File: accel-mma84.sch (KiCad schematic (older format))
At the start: 9 parts, among them J2 CONN_01X10, J3 CONN_01X02, U1 MMA8452Q

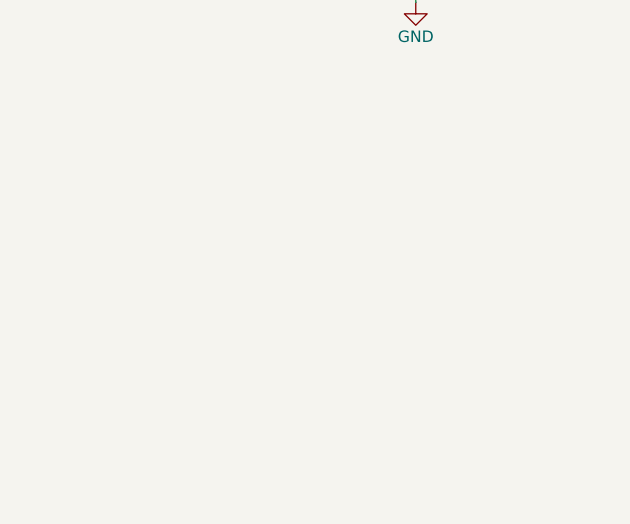
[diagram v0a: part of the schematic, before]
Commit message: Adds initial accelerometer draft.
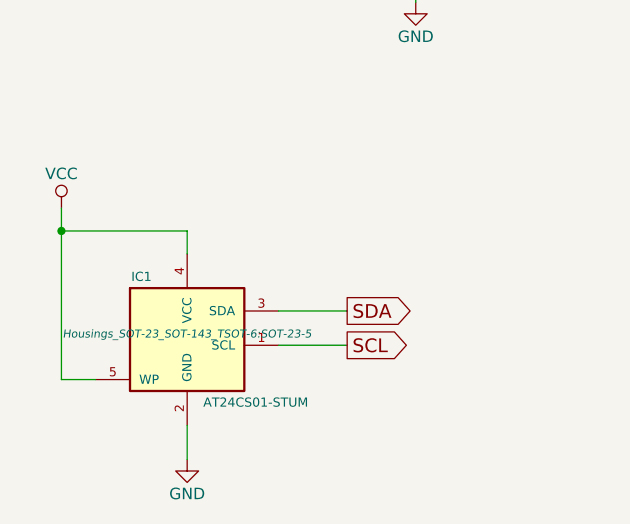
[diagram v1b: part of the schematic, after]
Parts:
- added IC1: AT24CS01-STUM, Housings_SOT-23_SOT-143_TSOT-6:SOT-23-5, symbol AT24CS01-STUM
- U1: footprint SMD_Packages:SO-16-L -> Housings_DFN_QFN:QFN-16-1EP_3x3mm_Pitch0.5mm
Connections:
- net GND: now also IC1.2 (GND)
- net SCL: now also IC1.1 (SCL)
- net SDA: now also IC1.3 (SDA)
- net VCC: now also IC1.4 (VCC), IC1.5 (WP)
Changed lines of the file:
@@
 LIBS:contrib
 LIBS:valves
+LIBS:accel-mma84-cache
 EELAYER 25 0
 EELAYER END
@@
 $EndDescr
 $Comp
-L VCC #PWR01
+L VCC #PWR2
 U 1 1 559814FE
 P 2300 2250
-F 0 "#PWR01" H 2300 2100 50  0001 C CNN
+F 0 "#PWR2" H 2300 2100 50  0001 C CNN
 F 1 "VCC" H 2300 2400 50  0000 C CNN
 F 2 "" H 2300 2250 60  0000 C CNN
@@
 $EndComp
 $Comp
-L GND #PWR02
+L GND #PWR3
 U 1 1 5598154A
 P 2300 2950
-F 0 "#PWR02" H 2300 2700 50  0001 C CNN
+F 0 "#PWR3" H 2300 2700 50  0001 C CNN
 F 1 "GND" H 2300 2800 50  0000 C CNN
 F 2 "" H 2300 2950 60  0000 C CNN
@@
 F 0 "U1" H 4700 3550 49  0000 C CNN
 F 1 "MMA8452Q" H 4950 2450 60  0000 C CNN
-F 2 "SMD_Packages:SO-16-L" H 4900 3000 60  0001 C CNN
+F 2 "Housings_DFN_QFN:QFN-16-1EP_3x3mm_Pitch0.5mm" H 4900 3000 60  0001 C CNN
 F 3 "" H 4900 3000 60  0000 C CNN
 	1    4900 3000
@@
 $EndComp
 $Comp
-L GND #PWR03
+L GND #PWR5
 U 1 1 5598173F
 P 3650 3750
-F 0 "#PWR03" H 3650 3500 50  0001 C CNN
+F 0 "#PWR5" H 3650 3500 50  0001 C CNN
 F 1 "GND" H 3650 3600 50  0000 C CNN
 F 2 "" H 3650 3750 60  0000 C CNN
@@
 Connection ~ 3650 3050
 $Comp
-L VCC #PWR04
+L VCC #PWR6
 U 1 1 559817AB
 P 4100 2050
-F 0 "#PWR04" H 4100 1900 50  0001 C CNN
+F 0 "#PWR6" H 4100 1900 50  0001 C CNN
 F 1 "VCC" H 4100 2200 50  0000 C CNN
 F 2 "" H 4100 2050 60  0000 C CNN
@@
 	6900 3400 6900 3750
 $Comp
-L GND #PWR05
+L GND #PWR8
 U 1 1 55981C37
 P 6900 3750
-F 0 "#PWR05" H 6900 3500 50  0001 C CNN
+F 0 "#PWR8" H 6900 3500 50  0001 C CNN
 F 1 "GND" H 6900 3600 50  0000 C CNN
 F 2 "" H 6900 3750 60  0000 C CNN
@@
 $EndComp
 $Comp
-L VCC #PWR06
+L VCC #PWR7
 U 1 1 55981C69
 P 6300 1550
-F 0 "#PWR06" H 6300 1400 50  0001 C CNN
+F 0 "#PWR7" H 6300 1400 50  0001 C CNN
 F 1 "VCC" H 6300 1700 50  0000 C CNN
 F 2 "" H 6300 1550 60  0000 C CNN
@@
 	8350 1750 8350 3200
 $Comp
-L GND #PWR07
+L GND #PWR9
 U 1 1 55982264
 P 8350 3200
-F 0 "#PWR07" H 8350 2950 50  0001 C CNN
+F 0 "#PWR9" H 8350 2950 50  0001 C CNN
 F 1 "GND" H 8350 3050 50  0000 C CNN
 F 2 "" H 8350 3200 60  0000 C CNN
@@
 $EndComp
 $Comp
-L VCC #PWR08
+L VCC #PWR10
 U 1 1 5598229C
 P 8550 1550
-F 0 "#PWR08" H 8550 1400 50  0001 C CNN
+F 0 "#PWR10" H 8550 1400 50  0001 C CNN
 F 1 "VCC" H 8550 1700 50  0000 C CNN
 F 2 "" H 8550 1550 60  0000 C CNN
@@
 Wire Wire Line
 	9750 2550 9000 2550
+$Comp
+L AT24CS01-STUM IC1
+U 1 1 55993BB7
+P 2650 5200
+F 0 "IC1" H 2450 5450 40  0000 C CNN
+F 1 "AT24CS01-STUM" H 2950 4900 40  0000 C CNN
+F 2 "Housings_SOT-23_SOT-143_TSOT-6:SOT-23-5" H 2650 5200 35  0000 C CIN
+F 3 "" H 2650 5200 60  0000 C CNN
+	1    2650 5200
+	1    0    0    -1
+$EndComp
+$Comp
+L VCC #PWR1
+U 1 1 55993C5B
+P 2100 4650
+F 0 "#PWR1" H 2100 4500 50  0001 C CNN
+F 1 "VCC" H 2100 4800 50  0000 C CNN
+F 2 "" H 2100 4650 60  0000 C CNN
+F 3 "" H 2100 4650 60  0000 C CNN
+	1    2100 4650
+	1    0    0    -1
+$EndComp
+$Comp
+L GND #PWR4
+U 1 1 55993C83
+P 2650 5750
+F 0 "#PWR4" H 2650 5500 50  0001 C CNN
+F 1 "GND" H 2650 5600 50  0000 C CNN
+F 2 "" H 2650 5750 60  0000 C CNN
+F 3 "" H 2650 5750 60  0000 C CNN
+	1    2650 5750
+	1    0    0    -1
+$EndComp
+Wire Wire Line
+	2250 5400 2100 5400
+Wire Wire Line
+	2100 5400 2100 4650
+Wire Wire Line
+	2650 4850 2650 4750
+Wire Wire Line
+	2650 4750 2100 4750
+Connection ~ 2100 4750
+Wire Wire Line
+	2650 5600 2650 5750
+Text GLabel 3350 5100 2    60   Output ~ 0
+SDA
+Text GLabel 3350 5250 2    60   Output ~ 0
+SCL
+Wire Wire Line
+	3050 5100 3350 5100
+Wire Wire Line
+	3350 5250 3050 5250
 $EndSCHEMATC
